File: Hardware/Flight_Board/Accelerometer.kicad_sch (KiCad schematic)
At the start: 1 part

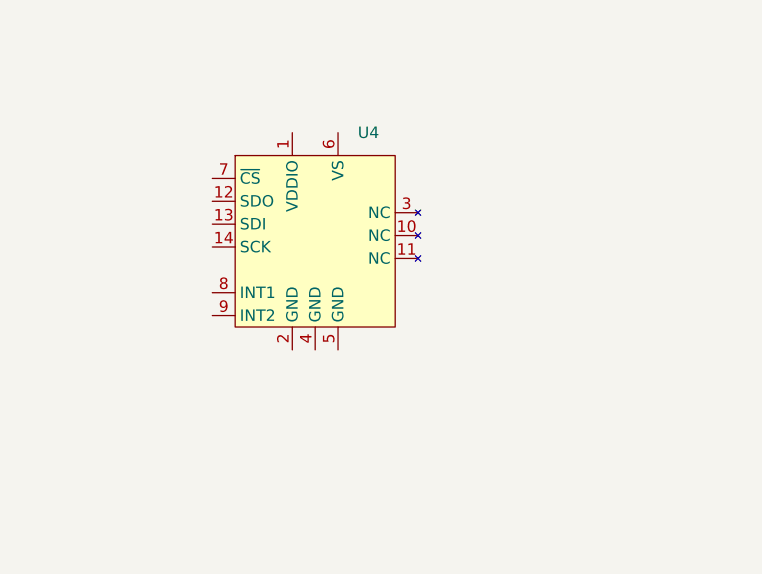
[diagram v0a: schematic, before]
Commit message: Added initial design for Accel.
Created initial schematics for accelerometer and VS headers on Page 2
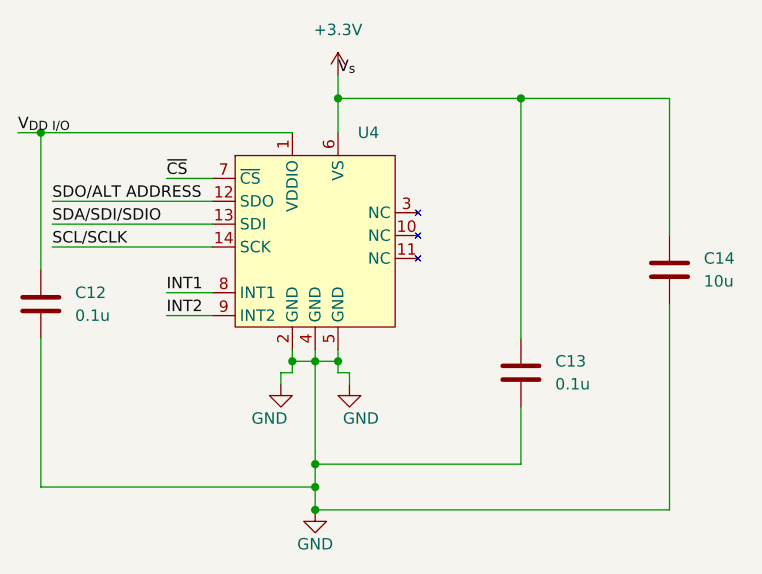
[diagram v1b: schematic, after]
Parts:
- added C12, C13: 0.1u, symbol Device:C
- added C14: 10u, symbol Device:C
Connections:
- net V_{DD I/O}: now reaches U4.1 (VDDIO)
- net V_{DD I/O}: now also C12.1
- net SDO/ALT ADDRESS: now reaches U4.12 (SDO)
- net SDA/SDI/SDIO: now reaches U4.13 (SDI)
- net SCL/SCLK: now reaches U4.14 (SCK)
- net GND: now reaches U4.2 (GND)
- net GND: now also U4.4 (GND), U4.5 (GND), C12.2, C13.2, C14.2
- net +3.3V: now reaches U4.6 (VS)
- net +3.3V: now also C13.1, C14.1
- net ~{CS}: now reaches U4.7 (~{CS})
- net INT1: now reaches U4.8 (INT1)
- net INT2: now reaches U4.9 (INT2)
